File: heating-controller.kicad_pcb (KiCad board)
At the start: 2 copper layers, 150 x 95 mm, 159 parts, among them J1 USB-C 16P, J110 MAINS IN L/N, J111 K1 L/COM/NO, J112 K2 L/COM/NO, J113 K3 L/COM/NO, J114 K4 L/COM/NO, J115 END SW 1/2/3, J116 DEMAND 230V/24V/RET, J201 OT (24V max), J3 FLOW, J4 OUTDOOR, J5 OLED, J6 QWIIC, J7 SPARE, J8 BOOT_JP, K101 HF32FA-G/005-HSL1, K102 HF32FA-G/005-HSL1, K103 HF32FA-G/005-HSL1, K104 HF32FA-G/005-HSL1 (DNP), Q101 AO3400A, Q102 AO3400A, Q103 AO3400A, Q104 AO3400A, Q201 S8550, SW1 RESET, SW2 BOOT, SW3 BTN1, SW4 BTN2, U1 ESP32-C6-WROOM-1-N8, U101 LTV-817S, U102 LTV-817S, U103 LTV-817S, U104 LTV-817S, U105 LTV-817S, U2 AMS1117-3.3, U201 LTV-817S (TX), U202 LTV-817S (RX), U3 USBLC6-2SC6

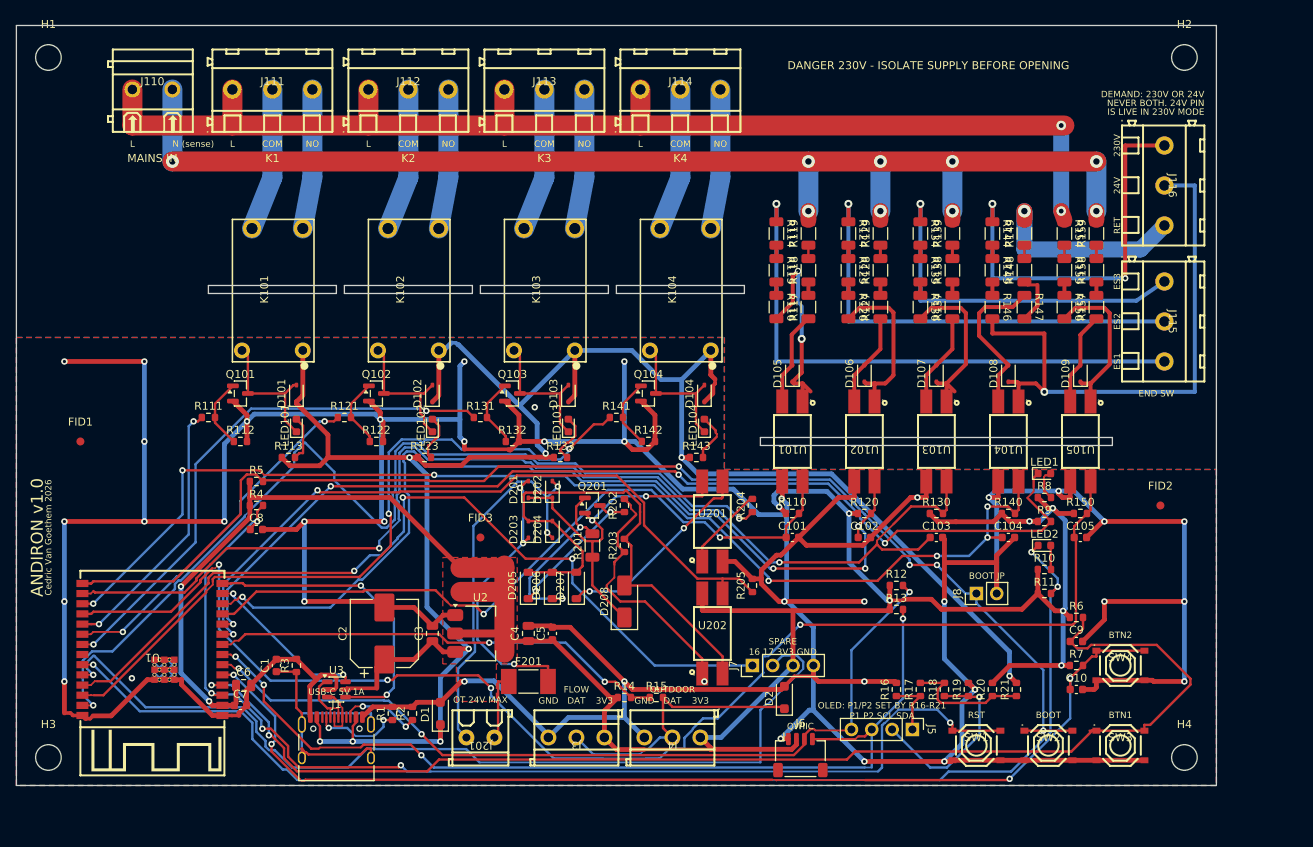
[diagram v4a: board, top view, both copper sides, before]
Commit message: Andiron v1.0 redesign: volt-free changeover relays, no mains sensing, layout by module area
- Relays: four HF115F/005-1ZS3A changeover relays (CH1-CH4), each with its own
  NC/COM/NO terminal, as UK heating controllers present their outputs; 5 kV
  VDE-reinforced coil-to-contact insulation. Each channel is its own net class
  and keeps 6.4 mm clearance and creepage from everything that is not itself.
- Removed the 230 V supply input, L/N rails and all five mains sensing inputs
  (30 resistors, 5 optos, end-switch and demand terminals). The only mains on
  the board is the relay contacts.
- Power: LDL1117S33R replaces the AMS1117 (0.35 V dropout, ceramic-stable,
  18 V abs-max, no heat-spreading copper); relays run from USB 5 V directly.
- OLED header fixed to GND/3V3/SCL/SDA (option resistors removed); freed GPIOs
  on an 8-pin spare header; Mains IO sheet renamed Relays.
- Layout regenerated by module area (relay strip, drivers, MCU with antenna at
  the left edge, power, OpenTherm, sensors, controls), 150 x 90 mm. Placement
  and shared geometry now in tools/layout/; tools/sync_netlist.py syncs the
  schematic to the board headlessly.
- Low-voltage clearance 0.25 mm so module pins escape straight out; USB nets
  get their own 0.2 mm class. Pipeline widens router neck-down stubs; stitching
  and island-repair vias avoid pads.
- Silkscreen relabelled in plain language (CH1 NC COM NO, OPENTHERM, FLOW TEMP,
  OUTDOOR TEMP, ...); repository URL removed.
- Docs: requirements and design brief rewritten for v1.0, schematic plan,
  README, BOM, renders, schematic PDF and layout lessons updated.

ERC 0 errors; DRC 0 errors, 0 unconnected, parity clean; sanity PASS.
BOM: ~$15.77 -> ~$24.03 components per board (~$28.97 -> ~$37.23 at 5 incl.
fees), mostly the four HF115F relays.

Co-Authored-By: Claude Opus 5.5 <noreply@anthropic.com>
Claude-Session: https://claude.ai/code/session_01XDSh2Z4phxf7z2Gu1153CL
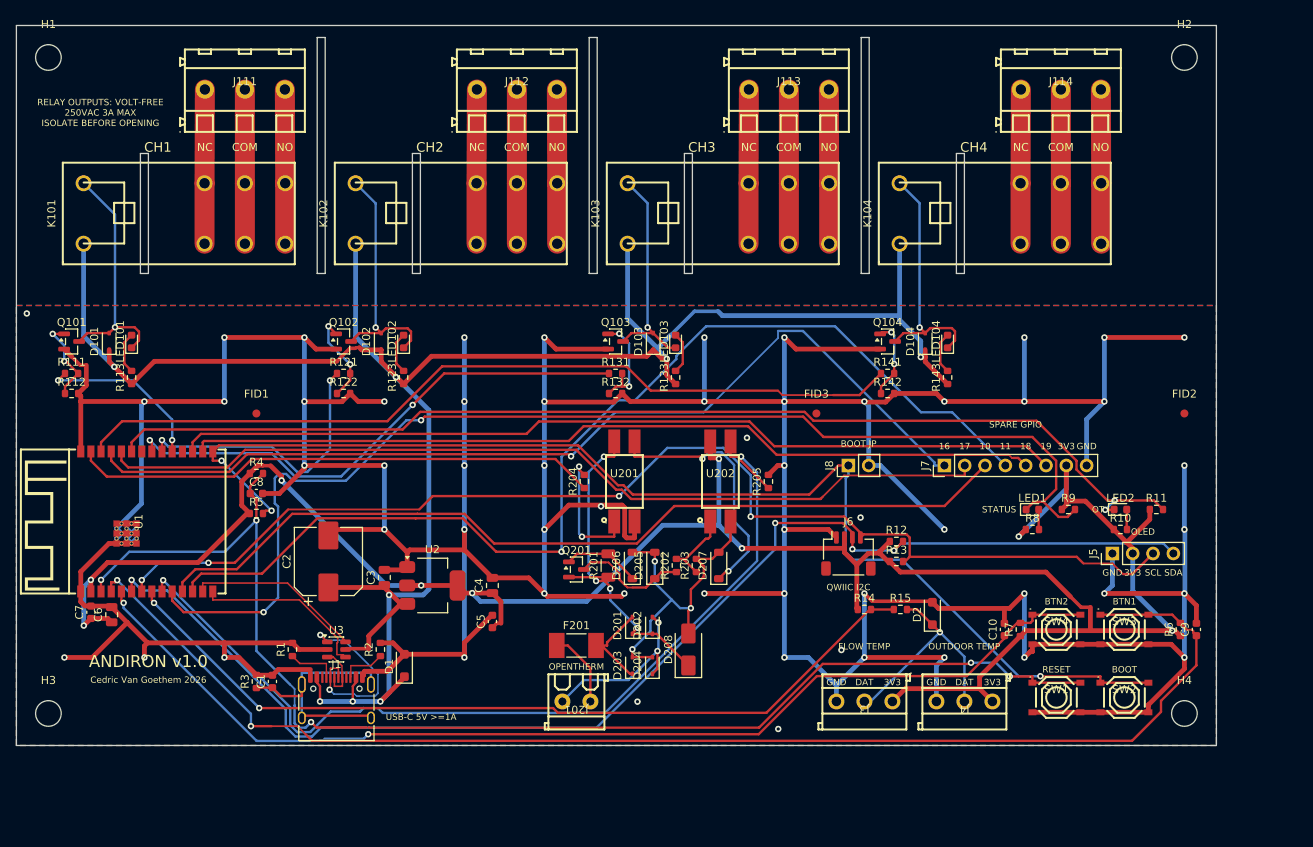
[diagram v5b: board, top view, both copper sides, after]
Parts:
- removed C101, C102, C103, C104, C105: 1uF, Capacitor_SMD:C_0603_1608Metric
- removed D105, D106, D107, D108, D109: 1N4148WS, Diode_SMD:D_SOD-323
- removed J110: MAINS IN L/N, jlc:CONN-TH_2P-P5.00_WJ128V-5.0-2P
- removed J115: END SW 1/2/3, jlc:CONN-TH_3P-P5.00_WJ128V-5.0-3P
- removed J116: DEMAND 230V/24V/RET, jlc:CONN-TH_3P-P5.00_WJ128V-5.0-3P
- removed R110, R120, R130, R140, R150: 220k, Resistor_SMD:R_0603_1608Metric
- removed R114, R115, R116, R117, R118, R119, R124, R125, R126, R127, R128, R129, R134, R135, R136, R137, R138, R139, R144, R145, R146, R147, R148, R149, R154, R155, R156, R157, R158, R159: 22k, Resistor_SMD:R_1206_3216Metric
- removed R16, R18, R20: 0R, Resistor_SMD:R_0603_1608Metric
- removed R17, R19, R21: 0R (DNP), Resistor_SMD:R_0603_1608Metric
- removed U101, U102, U103, U104, U105: LTV-817S, jlc:OPTO-SMD-4_L4.6-W6.5-P2.54-LS10.3-BL
- J5: value OLED -> OLED GND/3V3/SCL/SDA
- J7: value SPARE -> SPARE GPIO; footprint Connector_PinHeader_2.54mm:PinHeader_1x04_P2.54mm_Vertical -> Connector_PinHeader_2.54mm:PinHeader_1x08_P2.54mm_Vertical
- K101, K102, K103: value HF32FA-G/005-HSL1 -> HF115F/005-1ZS3A; footprint jlc:RELAY-TH_HF32FA-XX-HXX1X -> jlc:RELAY-TH_HF115F-024-2ZS4
- K104: value HF32FA-G/005-HSL1 (DNP) -> HF115F/005-1ZS3A; footprint jlc:RELAY-TH_HF32FA-XX-HXX1X -> jlc:RELAY-TH_HF115F-024-2ZS4
- U2: value AMS1117-3.3 -> LDL1117S33R
- moved J114 47.6 mm to (130.6, 8.00)
- moved FID3 44.8 mm to (100.0, 48.5)
- moved K104 41.1 mm to (123.0, 23.5)
- moved J4 36.8 mm to (118.5, 84.5)
- moved J3 36.3 mm to (106.0, 84.5)
- moved J7 34.7 mm to (116.0, 55.0)
- moved R141 34.3 mm to (108.9, 43.5)
- moved J5 33.3 mm to (137.0, 66.0), turned to 90 degrees
- moved R143 33.0 mm to (116.4, 44.0), turned to 90 degrees
- moved R15 32.4 mm to (110.5, 73.0)
- moved LED104 32.2 mm to (116.4, 39.5)
- moved R14 32.0 mm to (106.0, 73.0)
- moved Q104 30.6 mm to (108.9, 39.5)
- moved J113 30.6 mm to (96.6, 8.00)
- moved R142 30.5 mm to (108.9, 46.0)
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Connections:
- net /Mains IO/COIL1 renamed /Relays/COIL1
- net /Mains IO/COIL2 renamed /Relays/COIL2
- net /Mains IO/COIL3 renamed /Relays/COIL3
- net /Mains IO/COIL4 renamed /Relays/COIL4
- net /Mains IO/G1 renamed /Relays/G1
- net /Mains IO/G2 renamed /Relays/G2
- net /Mains IO/G3 renamed /Relays/G3
- net /Mains IO/G4 renamed /Relays/G4
- net /Mains IO/LEDR1 renamed /Relays/LEDR1
- net /Mains IO/LEDR2 renamed /Relays/LEDR2
- net /Mains IO/LEDR3 renamed /Relays/LEDR3
- net /Mains IO/LEDR4 renamed /Relays/LEDR4
- J111 pad 1: /Mains IO/MAINS_L -> /Relays/NC1
- J111 pad 2: /Mains IO/COM1 -> /Relays/COM1
- J111 pad 3: /Mains IO/NO1 -> /Relays/NO1
- J112 pad 1: /Mains IO/MAINS_L -> /Relays/NC2
- J112 pad 2: /Mains IO/COM2 -> /Relays/COM2
- J112 pad 3: /Mains IO/NO2 -> /Relays/NO2
- J113 pad 1: /Mains IO/MAINS_L -> /Relays/NC3
- J113 pad 2: /Mains IO/COM3 -> /Relays/COM3
- J113 pad 3: /Mains IO/NO3 -> /Relays/NO3
- J114 pad 1: /Mains IO/MAINS_L -> /Relays/NC4
- J114 pad 2: /Mains IO/COM4 -> /Relays/COM4
- J114 pad 3: /Mains IO/NO4 -> /Relays/NO4
- J5 pad 1: /Power + MCU/OLED_P1 -> GND
- J5 pad 2: /Power + MCU/OLED_P2 -> +3V3
- J7 pad 3: +3V3 -> /Power + MCU/IO10
- J7 pad 4: GND -> /Power + MCU/IO11
- K101 pad 3: /Mains IO/COM1 -> /Relays/NC1
- K101 pad 4: /Mains IO/NO1 -> /Relays/NC1
- K102 pad 3: /Mains IO/COM2 -> /Relays/NC2
- K102 pad 4: /Mains IO/NO2 -> /Relays/NC2
- K103 pad 3: /Mains IO/COM3 -> /Relays/NC3
- K103 pad 4: /Mains IO/NO3 -> /Relays/NC3
- K104 pad 3: /Mains IO/COM4 -> /Relays/NC4
- K104 pad 4: /Mains IO/NO4 -> /Relays/NC4
- U1 pad 11: /ES1 -> /Power + MCU/IO10
- U1 pad 12: /ES2 -> /Power + MCU/IO11
- U1 pad 16: /ES3 -> /Power + MCU/IO18
- U1 pad 17: /DEMAND_IN -> /Power + MCU/IO19
- U1 pad 18: /MAINS_OK -> unconnected-(U1-IO20-Pad18)
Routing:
- net /MAINS_OK: track 170.4 -> 0.00 mm, vias 4 -> 0
- net /Mains IO/MAINS_N: track 153.7 -> 0.00 mm, vias 9 -> 0
- net /Mains IO/MAINS_L: track 150.9 -> 0.00 mm, vias 2 -> 0
- net /DEMAND_IN: track 145.2 -> 0.00 mm, vias 7 -> 0
- net /ES3: track 142.5 -> 0.00 mm, vias 2 -> 0
- net /Power + MCU/IO11: track 0.00 -> 133.9 mm, vias 0 -> 1
- net /ES2: track 115.6 -> 0.00 mm, vias 4 -> 0
- net /Power + MCU/IO19: track 0.00 -> 111.2 mm
- net /Power + MCU/IO10: track 0.00 -> 110.6 mm
- net /Power + MCU/IO18: track 0.00 -> 106.9 mm
- net /ES1: track 89.7 -> 0.00 mm, vias 2 -> 0
- net /Mains IO/DEMAND_24: track 71.3 -> 0.00 mm, vias 1 -> 0
- net /Mains IO/ES1_IN: track 70.4 -> 0.00 mm, vias 1 -> 0
- net /OT_OUT: track 122.6 -> 66.1 mm, vias 2 -> 0
- net /Mains IO/ES2_IN: track 56.4 -> 0.00 mm, vias 1 -> 0
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- removed copper zone on F.Cu, net +3V3
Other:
- board size 150 x 95 mm -> 150 x 90 mm
- board text added: "10"
- board text added: "11"
- board text added: "16"
- board text added: "17"
- board text added: "18"
- board text added: "19"
- board text added: "250VAC 3A MAX"
- board text added: "CH1"
- board text added: "CH2"
- board text added: "CH3"
- board text added: "CH4"
- board text added: "FLOW TEMP"
- board text added: "ISOLATE BEFORE OPENING"
- board text added: "NC"
- board text added: "OLED"
- board text added: "OPENTHERM"
- board text added: "OT"
- board text added: "OUTDOOR TEMP"
- board text added: "QWIIC I2C"
- board text added: "RELAY OUTPUTS: VOLT-FREE"
- board text added: "RESET"
- board text added: "SCL"
- board text added: "SDA"
- board text added: "SPARE GPIO"
- board text added: "STATUS"
- board text added: "USB-C 5V >=1A"
- board text removed: "16 17 3V3 GND"
- board text removed: "230V"
- board text removed: "24V"
- board text removed: "DANGER 230V - ISOLATE SUPPLY BEFORE OPENING"
- board text removed: "DEMAND: 230V OR 24V"
- board text removed: "END SW"
- board text removed: "ES1"
- board text removed: "ES2"
- board text removed: "ES3"
- board text removed: "FLOW"
- board text removed: "IS LIVE IN 230V MODE"
- board text removed: "K1"
- board text removed: "K2"
- board text removed: "K3"
- board text removed: "K4"
- board text removed: "L"
- board text removed: "MAINS IN"
- board text removed: "N (sense)"
- board text removed: "NEVER BOTH. 24V PIN"
- board text removed: "OLED: P1/P2 SET BY R16-R21"
- board text removed: "OT 24V MAX"
- board text removed: "OUTDOOR"
- board text removed: "P1 P2 SCL SDA"
- board text removed: "QWIIC"
- board text removed: "RET"
- board text removed: "RST"
- board text removed: "SPARE"
- board text removed: "USB-C 5V 1A"
- board text removed: "github.com/Zepheus/opentherm_heating_controller"

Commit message: Wall-hanging layout, cheaper parts, OLED area
Layout (160 x 95 mm): the board hangs on a wall with every cable from below
or the left. Relay and OpenTherm terminals on the bottom edge, USB-C, FLOW,
OUTDOOR and Qwiic on the left edge, antenna at the top edge. The OLED module
stacks in landscape over a reserved top-right area.

Parts: TE RT314005 relays replace the HF115F (same body and pin grid,
reinforced 5 kV / 10 mm insulation, flux-proof so no washing after THT); AEM
MF2410F1.000TM fast fuse replaces the Bourns (same breaking capacity and
I2t, Bourns nearly out of stock); Basic 100 nF and 1 uF capacitors.
Per-board total at 5: $37.23 -> $27.86 (components $24.03 -> $15.86).

Tooling: locked +5V rail and supply feed (Freerouting would not route the
net), USB-C pre-routes drawn in the receptacle's own frame, router keep-outs
over the isolation slots, temporary zones stripped in a text pass, wider
pour-island repair, a pre-routing placement check, and sanity checks for
connector edges, no-cable edges and the OLED area.

Co-Authored-By: Claude Opus 5.5 <noreply@anthropic.com>
Claude-Session: https://claude.ai/code/session_01XDSh2Z4phxf7z2Gu1153CL
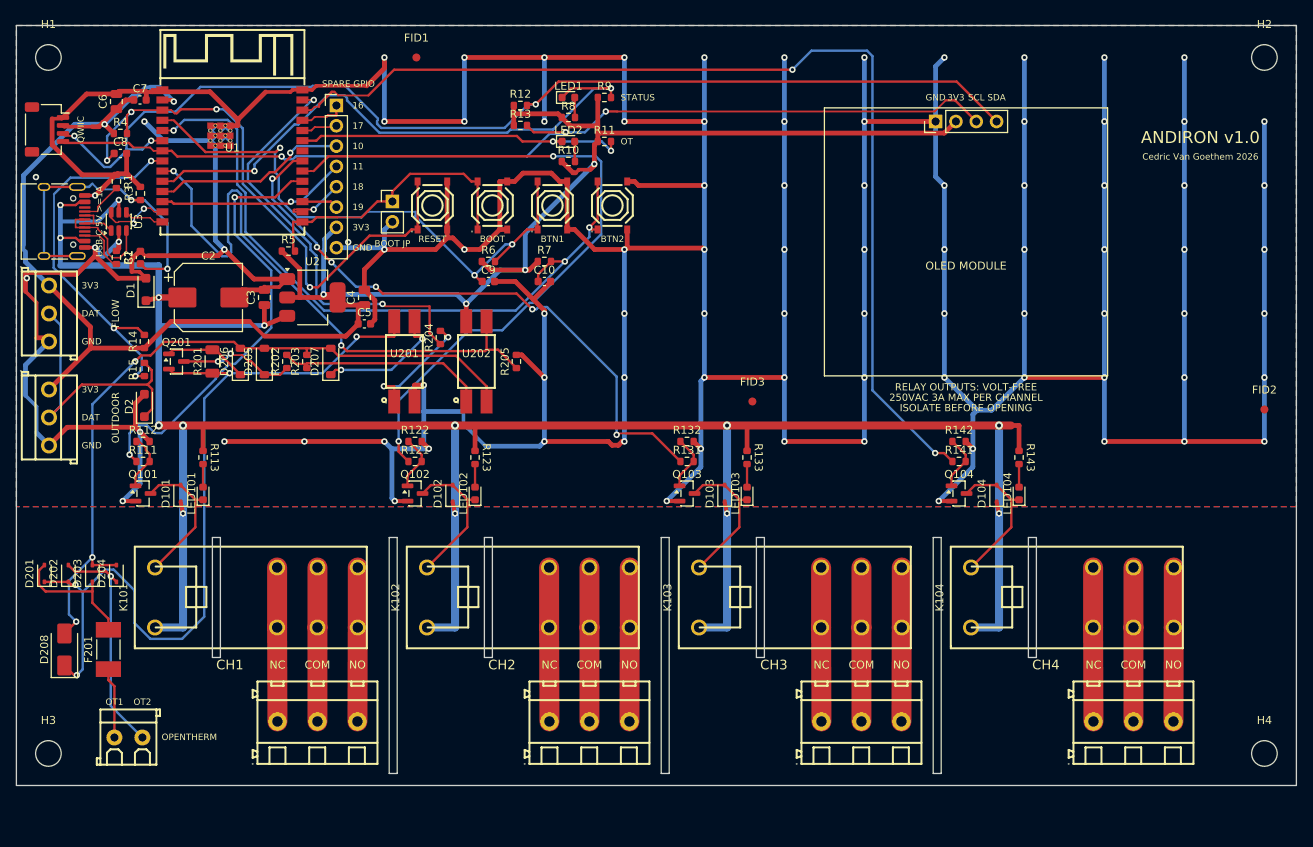
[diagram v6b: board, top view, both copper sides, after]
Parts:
- J111: value K1 L/COM/NO -> CH1 NC/COM/NO
- J112: value K2 L/COM/NO -> CH2 NC/COM/NO
- J113: value K3 L/COM/NO -> CH3 NC/COM/NO
- J114: value K4 L/COM/NO -> CH4 NC/COM/NO
- K101, K102, K103, K104: value HF115F/005-1ZS3A -> RT314005; footprint jlc:RELAY-TH_HF115F-024-2ZS4 -> jlc:RELAY-TH_RT314005_HF115F-PINS
- moved J4 119.8 mm to (4.08, 49.0), turned to -90 degrees
- moved J6 113.3 mm to (3.83, 13.0), turned to -90 degrees
- moved J3 112.9 mm to (4.08, 36.0), turned to -90 degrees
- moved D2 101.9 mm to (16.0, 47.5)
- moved SW2 100.1 mm to (59.5, 22.5), turned to 90 degrees
- moved SW1 99.3 mm to (52.0, 22.5), turned to 90 degrees
- moved R15 99.1 mm to (16.0, 43.0), turned to 90 degrees
- moved C9 98.6 mm to (59.0, 32.0), turned to 0 degrees
- moved R6 98.0 mm to (59.0, 29.5), turned to 0 degrees
- moved R14 96.0 mm to (16.0, 39.5), turned to 90 degrees
- moved SW3 89.0 mm to (67.0, 22.5), turned to 90 degrees
- moved J7 88.3 mm to (40.0, 10.0), turned to 0 degrees
- moved LED2 82.9 mm to (69.0, 14.5)
- moved R10 82.9 mm to (69.0, 17.0)
- moved R11 82.9 mm to (73.5, 14.5)
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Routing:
- net GND: track 746.5 -> 992.2 mm, vias 57 -> 88
- net /Power + MCU/BOOT: track 152.1 -> 36.4 mm, vias 3 -> 0
- net /Power + MCU/SPARE16: track 121.1 -> 5.75 mm, vias 1 -> 0
- net /Power + MCU/IO11: track 133.9 -> 23.8 mm
- net /Power + MCU/SPARE17: track 112.8 -> 4.59 mm
- net /Power + MCU/IO19: track 111.2 -> 4.53 mm
- net /Power + MCU/IO18: track 106.9 -> 7.91 mm, vias 0 -> 1
- net /Power + MCU/LED_OT: track 140.1 -> 41.9 mm
- net /Power + MCU/BTN1: track 167.8 -> 73.3 mm, vias 2 -> 3
- net /Power + MCU/EN: track 162.0 -> 72.9 mm, vias 5 -> 4
- net /Power + MCU/IO10: track 110.6 -> 24.4 mm, vias 0 -> 1
- net /Power + MCU/LED_STATUS: track 148.2 -> 73.2 mm
- net /OpenTherm/OT_VP: track 43.8 -> 105.6 mm
- net /Power + MCU/ONEWIRE: track 105.1 -> 48.3 mm, vias 2 -> 3
- net /RLY2: track 35.1 -> 89.5 mm
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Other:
- board size 150 x 90 mm -> 160 x 95 mm
- board text added: "250VAC 3A MAX PER CHANNEL"
- board text added: "FLOW"
- board text added: "OLED MODULE"
- board text added: "OT1"
- board text added: "OT2"
- board text added: "OUTDOOR"
- board text added: "QWIIC"
- board text removed: "250VAC 3A MAX"
- board text removed: "FLOW TEMP"
- board text removed: "OLED"
- board text removed: "OUTDOOR TEMP"
- board text removed: "QWIIC I2C"

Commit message: OLED on a Qwiic cable, boot jumper removed, enclosure re-sized
- J5 (OLED) is a Qwiic socket, same part as J6, in Qwiic order GND / 3V3 /
  SDA / SCL on GPIO6/GPIO7 (hardware I2C). The module sits in the cover
  window on a short cable (JST-SH to Dupont, or a soldered pigtail); the
  2.9 mm socket replaces a header that needed ~20 mm with Dupont housings.
- J8 (boot jumper) removed from schematic and board: the BOOT button does
  the same.
- Enclosure section rewritten: ~170 x 135 x 32 mm with a mains wiring bay
  (cable clamps, OT/mains rib), standoffs and support posts, USB-C wall
  relief, lid plungers for BTN1/BTN2.
- route_board.py no longer drops a stitching via that a GND track ends on
  (it disconnected a route after this re-route).
- Board re-routed; ERC/DRC/parity/sanity clean. 15 -> 13 Extended parts;
  estimate at 5 boards incl. fees $24.79 -> $23.76 per board.

Co-Authored-By: Claude Opus 5.5 <noreply@anthropic.com>
Claude-Session: https://claude.ai/code/session_01XDSh2Z4phxf7z2Gu1153CL
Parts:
- removed J8: BOOT_JP, Connector_PinHeader_2.54mm:PinHeader_1x02_P2.54mm_Vertical
- J5: value OLED GND/3V3/SCL/SDA -> OLED (Qwiic) GND/3V3/SDA/SCL; footprint Connector_PinHeader_2.54mm:PinHeader_1x04_P2.54mm_Vertical -> Connector_JST:JST_SH_SM04B-SRSS-TB_1x04-1MP_P1.00mm_Horizontal
- moved J5 3.83 mm to (118.7, 11.5), turned to 0 degrees
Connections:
- J5 pad 3: /Power + MCU/SCL -> /Power + MCU/SDA
- J5 pad 4: /Power + MCU/SDA -> /Power + MCU/SCL
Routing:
- net /RLY2: track 89.5 -> 57.1 mm
- net /OpenTherm/OT_GND: track 92.3 -> 115.1 mm, vias 3 -> 4
- net /Power + MCU/SCL: track 124.4 -> 144.6 mm, vias 3 -> 4
- net /OpenTherm/OT_VP: track 105.6 -> 89.3 mm, vias 4 -> 3
- net GND: track 992.2 -> 1006.9 mm, vias 88 -> 91
- net /Power + MCU/ONEWIRE: track 48.3 -> 35.0 mm, vias 3 -> 4
- net /Power + MCU/IO10: track 24.4 -> 35.8 mm
- net /Power + MCU/IO11: track 23.8 -> 34.6 mm
- net /Power + MCU/LED_STATUS: track 73.2 -> 63.5 mm
- net /OT_IN: track 76.1 -> 85.5 mm
- net /RLY3: track 76.8 -> 70.4 mm, vias 6 -> 2
- net /RLY1: track 55.5 -> 49.1 mm
- net +3V3: track 263.6 -> 258.1 mm, vias 6 -> 4
- net /RLY4: track 130.6 -> 125.3 mm
- net /Power + MCU/BTN2: track 87.9 -> 83.7 mm
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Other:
- board text added: "OLED QWIIC"
- board text removed: "BOOT JP"
- board text removed: "SCL"
- board text removed: "SDA"
